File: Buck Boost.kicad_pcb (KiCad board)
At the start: 2 copper layers, 160 x 100 mm, 57 parts, among them J1 Pin_D1.2mm_L10.2mm_W2.9mm_Fla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, J1 Screw_Terminal_01x02, J2 Pin_D1.2mm_L10.2mm_W2.9mm_Fla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, J2 Screw_Terminal_01x02, J3 Pin_D1.2mm_L10.2mm_W2.9mm_Fla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, J3 Screw_Terminal_01x02, J4 Pin_D1.2mm_L10.2mm_W2.9mm_Fla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, J6 Pin_D1.2mm_L10.2mm_W2.9mm_Fla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, J7 Pin_D1.2mm_L10.2mm_W2.9mm_Fla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, K1 SW_SPDT, K2 Jumper_2_Bridged, T1 IRF4905, T2 IRF4905, U1 HCPL-3120, U2 arduino, U3 HCPL-3120

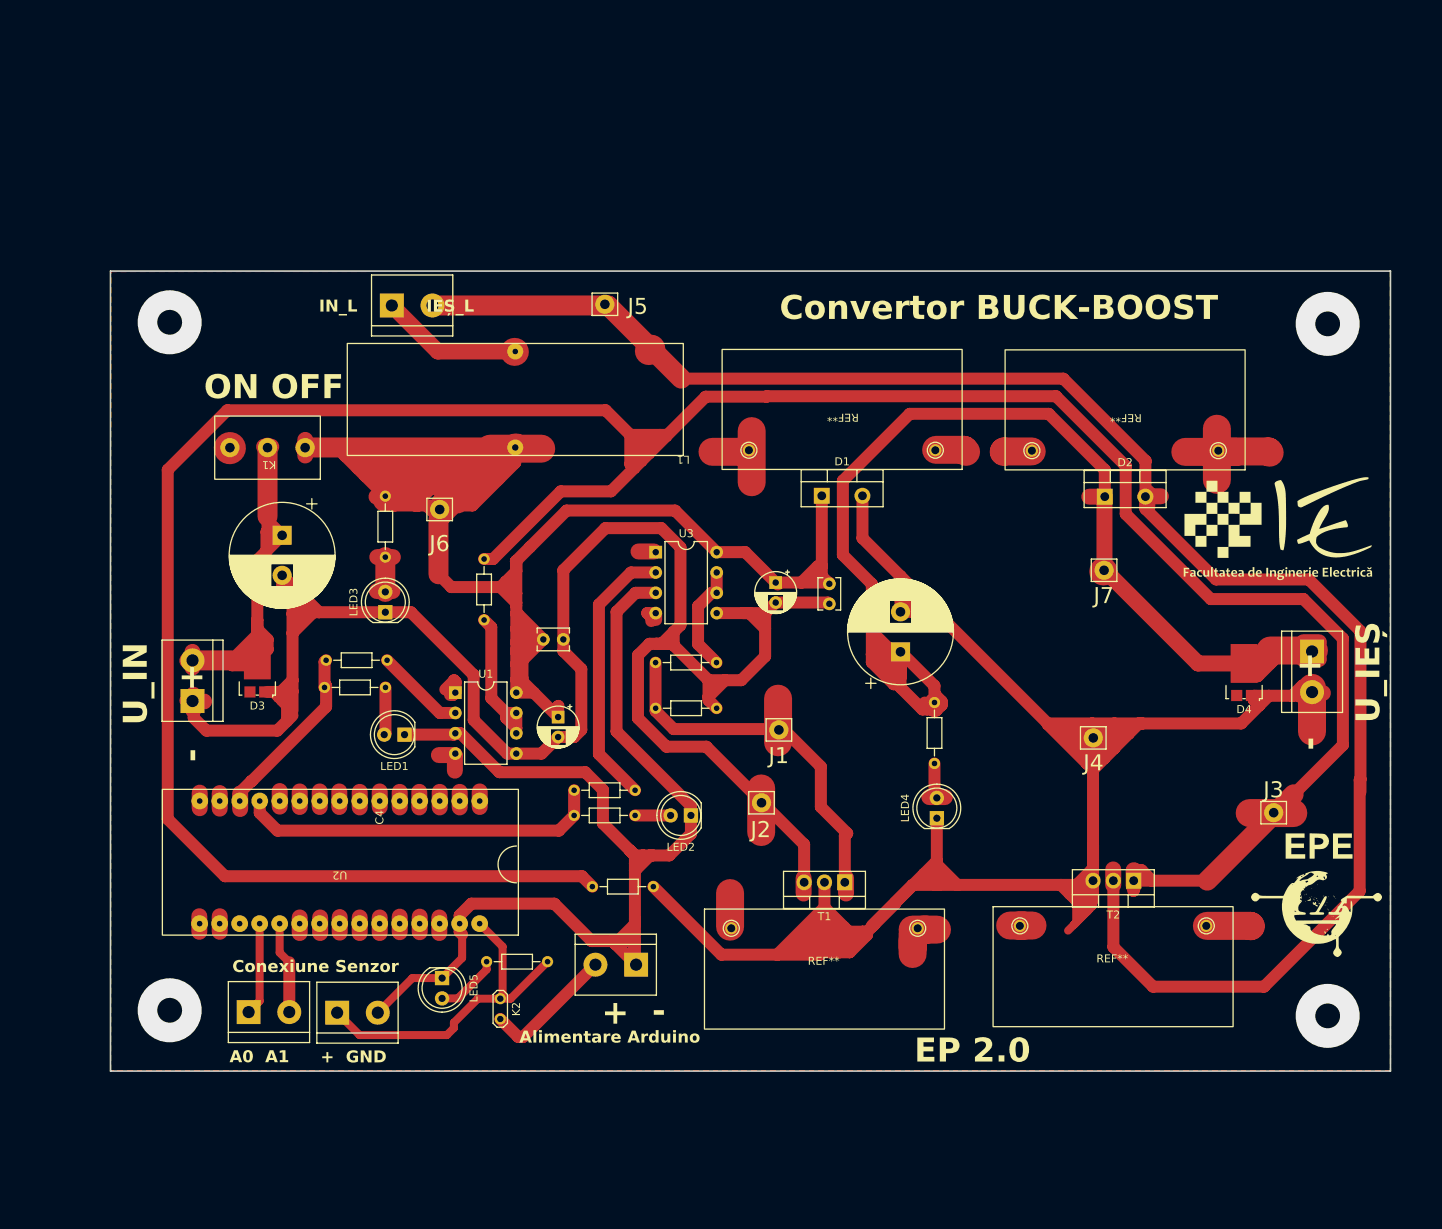
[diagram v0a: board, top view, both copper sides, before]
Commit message: sters PCB u vechi + adaugat niste footprints + mutat power truco
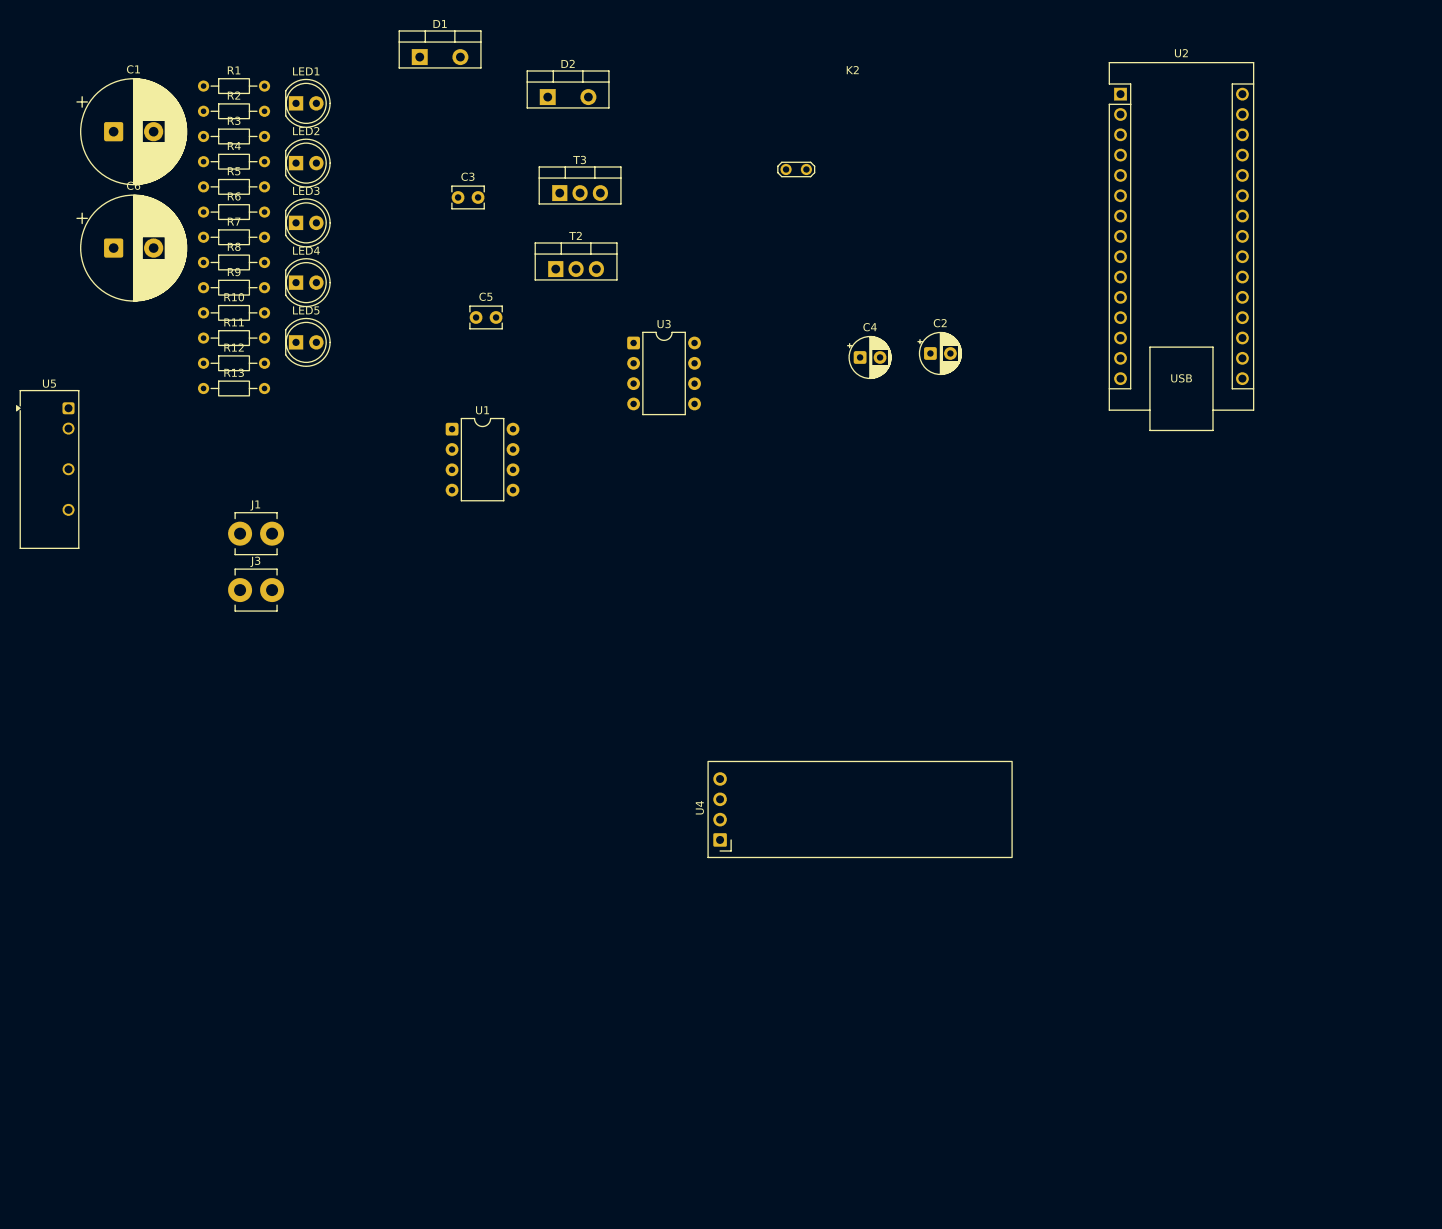
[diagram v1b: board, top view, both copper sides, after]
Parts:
- removed ?: 220uF, Capacitor_THT:CP_Radial_D13.0mm_P5.00mm
- removed ?: 100nF, Capacitor_THT:C_Disc_D3.8mm_W2.6mm_P2.50mm
- removed D3, D4: BAT54W, Schottky:Schottky
- removed G*** (x3): LOGO, Librarii Norbi:epe
- removed G*** (x2): LOGO, Librarii Norbi:Logo ie 1
- removed G***: LOGO, Librarii Norbi:epe utcluj
- removed the J1 at (57.1, 99.4)
- removed the J1 at (130.3, 103.0)
- removed J2: Screw_Terminal_01x02, TerminalBlock:TerminalBlock_bornier-2_P5.08mm
- removed J2, J4, J6, J7: Pin_D1.2mm_L10.2mm_W2.9mm_FlatFork, Connector_Pin:Pin_D1.2mm_L10.2mm_W2.9mm_FlatFork
- removed the J3 at (82.0, 50.0)
- removed the J3 at (197.0, 93.2)
- removed the J3 at (75.1, 138.4)
- removed the J3 at (192.2, 113.4)
- removed the J3 at (64.1, 138.3)
- removed K1: SW_SPDT, K1:TSM102A2
- removed L1: L, Bobina:bobina
- removed REF** (x4): Radiator, TLP350:Radiator
- removed REF**: J5, Connector_Pin:Pin_D1.2mm_L10.2mm_W2.9mm_FlatFork
- removed T1: IRF4905, Package_TO_SOT_THT:TO-220-3_Vertical
- added C3: C, Capacitor_THT:C_Disc_D3.8mm_W2.6mm_P2.50mm, F.Cu at (90.2, 36.5)
- added C6: CP1, Capacitor_THT:CP_Radial_D13.0mm_P5.00mm, F.Cu at (47.2, 42.8)
- added J1: Screw_Terminal_01x02, TerminalBlock_MetzConnect:TerminalBlock_MetzConnect_360381_1x01_Horizontal_ScrewM3.0, F.Cu at (63.0, 78.5)
- added J3: Screw_Terminal_01x02, TerminalBlock_MetzConnect:TerminalBlock_MetzConnect_360381_1x01_Horizontal_ScrewM3.0, F.Cu at (63.0, 85.6)
- added R12: R, Resistor_THT:R_Axial_DIN0204_L3.6mm_D1.6mm_P7.62mm_Horizontal, F.Cu at (58.4, 57.2)
- added R13: R, Resistor_THT:R_Axial_DIN0204_L3.6mm_D1.6mm_P7.62mm_Horizontal, F.Cu at (58.4, 60.4)
- added T3: IRF4905, Package_TO_SOT_THT:TO-220-3_Vertical, F.Cu at (103.0, 36.0)
- added U4: ER_OLEDM0.91_1x-I2C, Display:ER_OLEDM0.91_1x-I2C, F.Cu at (123.0, 116.8)
- added U5: TMA-1512S, Converter_DCDC:Converter_DCDC_TRACO_TMA-15xxS_24xxS_Single_THT, F.Cu at (41.6, 62.9)
- C1: value 220uF -> CP1
- C2: value 10uF -> CP1
- C5: value 100nF -> C
- R1, R11, R2, R3, R4: value 200 -> R
- R10, R6, R8: value 10k -> R
- R5: value 3k -> R
- R7, R9: value 22 -> R
- U2: footprint arduino:Arduino -> Module:Arduino_Nano
- moved U2 136.9 mm to (173.1, 23.6), turned to 0 degrees
- moved R6 114.4 mm to (58.4, 38.3), turned to 0 degrees
- moved K2 109.6 mm to (131.2, 33.0), turned to 0 degrees
- moved T2 105.2 mm to (102.5, 45.5), turned to 0 degrees
- moved LED4 104.4 mm to (70.0, 47.1), turned to 0 degrees
- moved R3 96.7 mm to (58.4, 28.9)
- moved LED2 95.3 mm to (70.0, 32.2), turned to 0 degrees
- moved R4 91.2 mm to (58.4, 32.0)
- moved R10 91.1 mm to (58.4, 50.9), turned to 0 degrees
- moved R11 89.0 mm to (58.4, 54.1), turned to 0 degrees
- moved D2 85.7 mm to (101.5, 23.9)
- moved R8 85.0 mm to (58.4, 44.6), turned to 0 degrees
- moved R7 83.3 mm to (58.4, 41.5), turned to 0 degrees
- moved LED5 81.5 mm to (70.0, 54.6), turned to 0 degrees
- moved LED1 80.1 mm to (70.0, 24.7), turned to 0 degrees
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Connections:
- C1 pad 2: Net-(C1-Pad2) -> Net-(D1-A)
- C2 pad 1: Net-(C2-Pad1) -> Net-(K1-A)
- C2 pad 2: Net-(C1-Pad2) -> Net-(D1-A)
- C4 pad 1: Net-(C2-Pad1) -> Net-(U3-VCC)
- C4 pad 2: Net-(C1-Pad2) -> Net-(U3-VEE)
- C5 pad 1: Net-(C2-Pad1) -> Net-(U3-VCC)
- C5 pad 2: Net-(C1-Pad2) -> Net-(U3-VEE)
- D1 pad 1: Net-(C2-Pad1) -> Net-(D1-K)
- D1 pad 2: Net-(C6-Pad2) -> Net-(D1-A)
- LED3 pad 1: Net-(C1-Pad2) -> Net-(D1-A)
- LED4 pad 1: Net-(C6-Pad2) -> Net-(D1-A)
- R10 pad 1: Net-(C6-Pad2) -> Net-(D1-A)
- R5 pad 1: Net-(C2-Pad1) -> Net-(K1-A)
- R8 pad 1: Net-(C1-Pad2) -> Net-(D1-A)
- T2 pad 3: Net-(C6-Pad2) -> Net-(D1-A)
- U1 pad 5: Net-(C1-Pad2) -> Net-(D1-A)
- U1 pad 8: Net-(C2-Pad1) -> Net-(K1-A)
- U2 pad 22: unconnected-(U2-Pad22) -> Net-(U2-A5)
- U2 pad 23: unconnected-(U2-Pad23) -> Net-(U2-A4)
- U2 pad 29: unconnected-(U2-Pad29) -> Net-(U2-3V3)
- U3 pad 5: Net-(C1-Pad2) -> Net-(U3-VEE)
- U3 pad 8: Net-(C2-Pad1) -> Net-(U3-VCC)
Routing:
- net Net-(T2-G): track 368.0 -> 0.00 mm
- net Net-(C6-Pad2): track 345.3 -> 0.00 mm
- net Net-(C2-Pad1): track 344.8 -> 0.00 mm
- net Net-(C1-Pad2): track 265.6 -> 0.00 mm
- net Net-(D2-A): track 241.3 -> 0.00 mm
- net Net-(D2-K): track 185.7 -> 0.00 mm
- net Net-(J2-Pin_1): track 157.3 -> 0.00 mm
- net Net-(D3-K): track 61.7 -> 0.00 mm
- net (no net): track 58.2 -> 0.00 mm, vias 4 -> 0
- net Net-(T3-G): track 52.9 -> 0.00 mm
- net Net-(U2-D9): track 45.6 -> 0.00 mm
- net Net-(K2-A): track 42.3 -> 0.00 mm
- net Net-(U3-A): track 33.8 -> 0.00 mm
- net Net-(U2-D10): track 24.6 -> 0.00 mm
- net Net-(R9-Pad1): track 19.0 -> 0.00 mm
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- removed copper zone on F.Cu, net (none)
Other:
- board outline removed
- board text removed: "+ GND"
- board text removed: "- +"
- board text removed: "A0 A1"
- board text removed: "Alimentare Arduino"
- board text removed: "Conexiune Senzor"
- board text removed: "Convertor BUCK-BOOST"
- board text removed: "EP 2.0"
- board text removed: "IN_L IEȘ_L"
- board text removed: "ON OFF"
- board text removed: "POPUSOIU CORNELIU"
- board text removed: "SZEKELY NORBERT CSABA"
- board text removed: "U_IEȘ"
- board text removed: "U_IN"

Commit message: V0.1
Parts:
- added C9: 1uF, Capacitor_THT:C_Disc_D3.8mm_W2.6mm_P2.50mm, F.Cu at (94.9, 150.8)
- added HS1: Heatsink_Pad_2Pin, Heatsink_laborator:Heasink_lab, F.Cu at (139.5, 92.5)
- added HS2: Heatsink_Pad_2Pin, Heatsink_laborator:Heasink_lab, F.Cu at (190.3, 114.0)
- added HS3: Heatsink_Pad_2Pin, Heatsink_laborator:Heasink_lab, F.Cu at (190.3, 83.0)
- added HS4: Heatsink_Pad_2Pin, Heatsink_laborator:Heasink_lab, F.Cu at (139.5, 123.0)
- added J2: Screw_Terminal_01x02, TerminalBlock:TerminalBlock_MaiXu_MX126-5.0-02P_1x02_P5.00mm, F.Cu at (74.4, 147.8)
- added J4: Screw_Terminal_01x02, TerminalBlock:TerminalBlock_MaiXu_MX126-5.0-02P_1x02_P5.00mm, F.Cu at (69.2, 75.3)
- added K1: SW_SPDT, Switch:SwitchMTS-Electronica, F.Cu at (84.0, 83.3)
- added L1: L, Bobina:Bobina 470uH 3A, F.Cu at (165.2, 61.5)
- added LED7: CQY99, LED_THT:LED_D5.0mm_IRGrey, F.Cu at (81.5, 65.6)
- added R15: R, Resistor_THT:R_Axial_DIN0204_L3.6mm_D1.6mm_P7.62mm_Horizontal, F.Cu at (76.5, 62.8)
- J1, J3: footprint TerminalBlock_MetzConnect:TerminalBlock_MetzConnect_360381_1x01_Horizontal_ScrewM3.0 -> TerminalBlock:TerminalBlock_MaiXu_MX126-5.0-02P_1x02_P5.00mm
- moved C6 136.1 mm to (168.8, 104.0), turned to 180 degrees
- moved R6 134.0 mm to (167.9, 115.5)
- moved R12 128.8 mm to (165.7, 128.5)
- moved K2 123.3 mm to (86.4, 147.8), turned to 180 degrees
- moved D2 122.5 mm to (181.8, 116.5), turned to -90 degrees
- moved R13 119.3 mm to (161.5, 120.4), turned to -90 degrees
- moved J3 119.2 mm to (168.2, 141.5), turned to 180 degrees
- moved D1 118.8 mm to (147.9, 120.0), turned to 90 degrees
- moved R10 115.1 mm to (166.7, 90.0)
- moved LED4 114.8 mm to (162.2, 115.5)
- moved R9 114.6 mm to (166.7, 85.5)
- moved U2 114.4 mm to (110.2, 119.2), turned to -90 degrees
- moved R8 113.0 mm to (158.8, 96.5), turned to 180 degrees
- moved R7 109.1 mm to (148.0, 103.8), turned to 90 degrees
- moved R11 98.5 mm to (89.2, 147.6), turned to 90 degrees
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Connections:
- C1 pad 1: Net-(D3-K) -> Net-(J1-Pin_2)
- C2 pad 1: Net-(K1-A) -> Net-(J4-Pin_2)
- C2 pad 2: Net-(D1-A) -> Net-(J4-Pin_1)
- C3 pad 1: Net-(K1-A) -> Net-(J4-Pin_2)
- C3 pad 2: Net-(D1-A) -> Net-(J4-Pin_1)
- C4 pad 2: Net-(U3-VEE) -> Net-(D1-K)
- C5 pad 2: Net-(U3-VEE) -> Net-(D1-K)
- U1 pad 5: Net-(D1-A) -> Net-(J4-Pin_1)
- U1 pad 8: Net-(K1-A) -> Net-(J4-Pin_2)
- U3 pad 5: Net-(U3-VEE) -> Net-(D1-K)
- U5 pad 1: Net-(K1-A) -> Net-(J4-Pin_2)
- U5 pad 2: Net-(D1-A) -> Net-(J4-Pin_1)
- U5 pad 4: Net-(U3-VEE) -> Net-(D1-K)
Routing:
- net Net-(D1-A): track 0.00 -> 274.5 mm, vias 0 -> 1
- net Net-(D1-K): track 0.00 -> 180.6 mm, vias 0 -> 2
- net Net-(J2-Pin_1): track 0.00 -> 172.3 mm, vias 0 -> 2
- net Net-(R9-Pad1): track 0.00 -> 128.4 mm, vias 0 -> 2
- net Net-(K1-A): track 0.00 -> 95.7 mm, vias 0 -> 1
- net Net-(J4-Pin_2): track 0.00 -> 92.3 mm, vias 0 -> 1
- net Net-(R7-Pad1): track 0.00 -> 88.9 mm, vias 0 -> 1
- net Net-(J4-Pin_1): track 0.00 -> 82.6 mm, vias 0 -> 2
- net Net-(D2-A): track 0.00 -> 74.5 mm
- net Net-(U2-A0): track 0.00 -> 73.7 mm
- net Net-(U3-A): track 0.00 -> 59.4 mm, vias 0 -> 1
- net Net-(D2-K): track 0.00 -> 50.0 mm
- net Net-(U2-3V3): track 0.00 -> 29.8 mm
- net Net-(J1-Pin_2): track 0.00 -> 29.2 mm
- net Net-(U1-A): track 0.00 -> 25.9 mm
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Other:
- board outline added: 145 x 102.5 mm
- board text added: "Okochi Nikolas Gabriel Rechesan Rares"

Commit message: master
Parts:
- added Dreapta1: SW_Push, Button_Switch_THT:SW_PUSH_6mm_H5mm, F.Cu at (124.8, 157.5)
- added J5: Screw_Terminal_01x02, TerminalBlock:TerminalBlock_MaiXu_MX126-5.0-02P_1x02_P5.00mm, F.Cu at (134.0, 59.0)
- added Jos1: SW_Push, Button_Switch_THT:SW_PUSH_6mm_H5mm, F.Cu at (116.3, 157.5)
- added Stanga1: SW_Push, Button_Switch_THT:SW_PUSH_6mm_H5mm, F.Cu at (99.2, 157.5)
- added Sus1: SW_Push, Button_Switch_THT:SW_PUSH_6mm_H5mm, F.Cu at (107.8, 157.5)
- moved J3 12.7 mm to (169.2, 154.2)
- moved J1 5.45 mm to (66.0, 92.8)
- moved J4 3.20 mm to (66.0, 75.2)
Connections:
- HS1 pad 2: unconnected-(HS1-Pad1) -> unconnected-(HS1-Pad2)
- HS2 pad 2: unconnected-(HS2-Pad1) -> unconnected-(HS2-Pad2)
- HS3 pad 2: unconnected-(HS3-Pad1) -> unconnected-(HS3-Pad2)
- HS4 pad 2: unconnected-(HS4-Pad1) -> unconnected-(HS4-Pad2)
- L1 pad 1: Net-(D1-K) -> Net-(J5-Pin_2)
- U2 pad 5: unconnected-(U2-D2-Pad5) -> Net-(U2-D2)
- U2 pad 6: unconnected-(U2-D3-Pad6) -> Net-(U2-D3)
- U2 pad 7: unconnected-(U2-D4-Pad7) -> Net-(U2-D4)
- U2 pad 8: unconnected-(U2-D5-Pad8) -> Net-(U2-D5)
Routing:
- net Net-(J2-Pin_1): track 172.3 -> 275.6 mm, vias 2 -> 5
- net Net-(U2-D5): track 0.00 -> 51.9 mm, vias 0 -> 1
- net Net-(U2-D2): track 0.00 -> 47.7 mm
- net Net-(U2-D3): track 0.00 -> 45.3 mm, vias 0 -> 1
- net Net-(U2-D4): track 0.00 -> 44.9 mm, vias 0 -> 1
- net Net-(J5-Pin_2): track 0.00 -> 27.5 mm
- net Net-(D2-K): track 50.0 -> 68.4 mm, vias 0 -> 1
- net Net-(U2-D9): track 17.0 -> 35.4 mm, vias 1 -> 2
- net Net-(D1-A): track 274.5 -> 288.3 mm, vias 1 -> 3
- net Net-(D1-K): track 180.6 -> 191.2 mm
- net Net-(J1-Pin_2): track 29.2 -> 38.6 mm, vias 0 -> 1
- net Net-(J4-Pin_2): track 92.3 -> 100.1 mm
- net Net-(U2-D10): track 11.2 -> 17.2 mm, vias 0 -> 1
- net Net-(R9-Pad1): track 128.4 -> 132.4 mm
- net Net-(U2-3V3): track 29.8 -> 33.3 mm
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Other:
- board size 145 x 102.5 mm -> 145 x 107.2 mm
- board text added: "+"
- board text added: "D10"
- board text added: "D9"
- board text added: "GND"
- board text added: "Iesire"
- board text added: "Intrare"
- board text added: "Vout"
- board text added: "_"
